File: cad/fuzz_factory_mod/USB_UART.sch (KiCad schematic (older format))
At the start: 14 parts, among them J301 USB_B_Micro, U301 USBLC6-2SC6, U302 FT230XS

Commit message: Continued schematic.
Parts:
- U301: footprint Package_TO_SOT_SMD:SOT-23-6 -> TO_SOT_Packages_SMD:SOT-23-6
- U302: footprint Package_SO:SSOP-16_3.9x4.9mm_P0.635mm -> Housings_SSOP:SSOP-16_3.9x4.9mm_Pitch0.635mm
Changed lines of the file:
@@
 $Descr A4 11693 8268
 encoding utf-8
-Sheet 3 22
+Sheet 3 26
 Title ""
 Date ""
@@
 F 0 "U302" H 5550 4150 50  0000 C CNN
 F 1 "FT230XS" H 6400 2950 50  0000 C CNN
-F 2 "Package_SO:SSOP-16_3.9x4.9mm_P0.635mm" H 6500 2900 50  0001 C CNN
+F 2 "Housings_SSOP:SSOP-16_3.9x4.9mm_Pitch0.635mm" H 6500 2900 50  0001 C CNN
 F 3 "http://www.ftdichip.com/Products/ICs/FT230X.html" H 6050 3550 50  0001 C CNN
 	1    6050 3550
@@
 F 0 "U301" V 2500 3750 50  0000 C CNN
 F 1 "USBLC6-2SC6" V 3200 3950 50  0000 C CNN
-F 2 "Package_TO_SOT_SMD:SOT-23-6" H 2100 3900 50  0001 C CNN
+F 2 "TO_SOT_Packages_SMD:SOT-23-6" H 2100 3900 50  0001 C CNN
 F 3 "http://www2.st.com/resource/en/datasheet/CD00050750.pdf" H 3050 3850 50  0001 C CNN
 	1    2850 3500

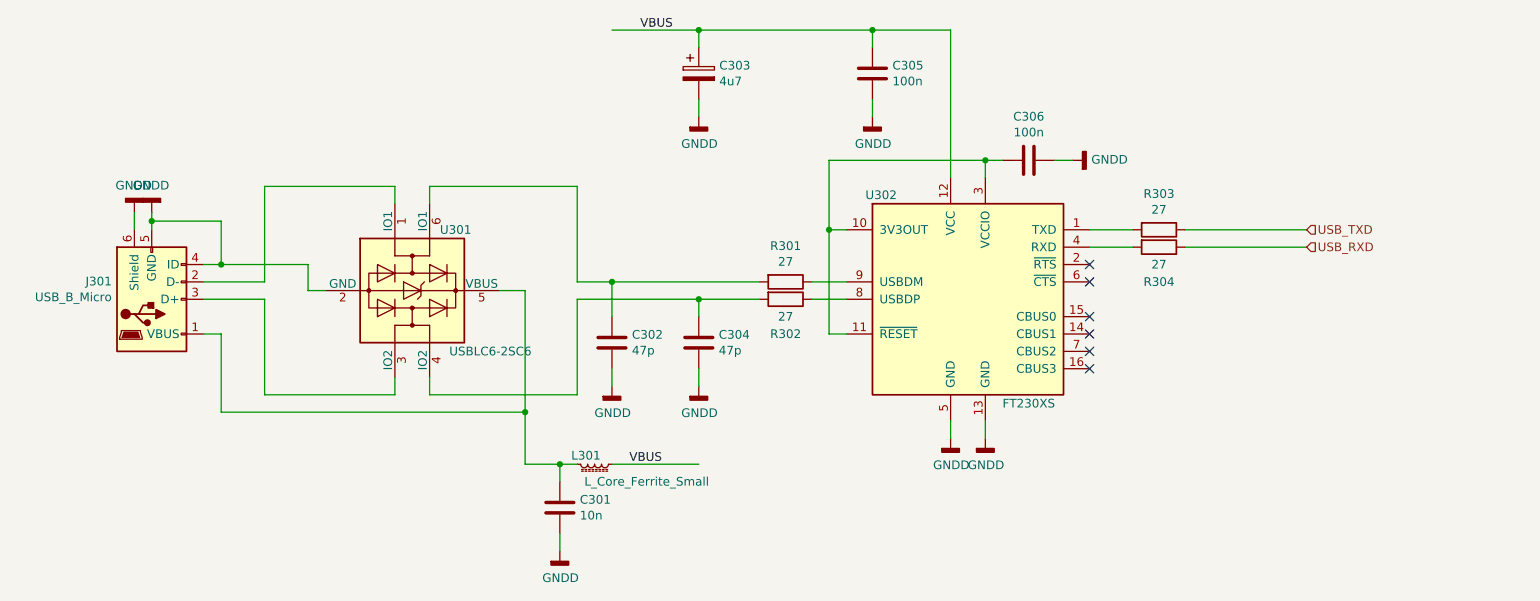
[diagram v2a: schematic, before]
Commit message: Changes architecture.
Corrections on schematic.
Continued Layout placement.
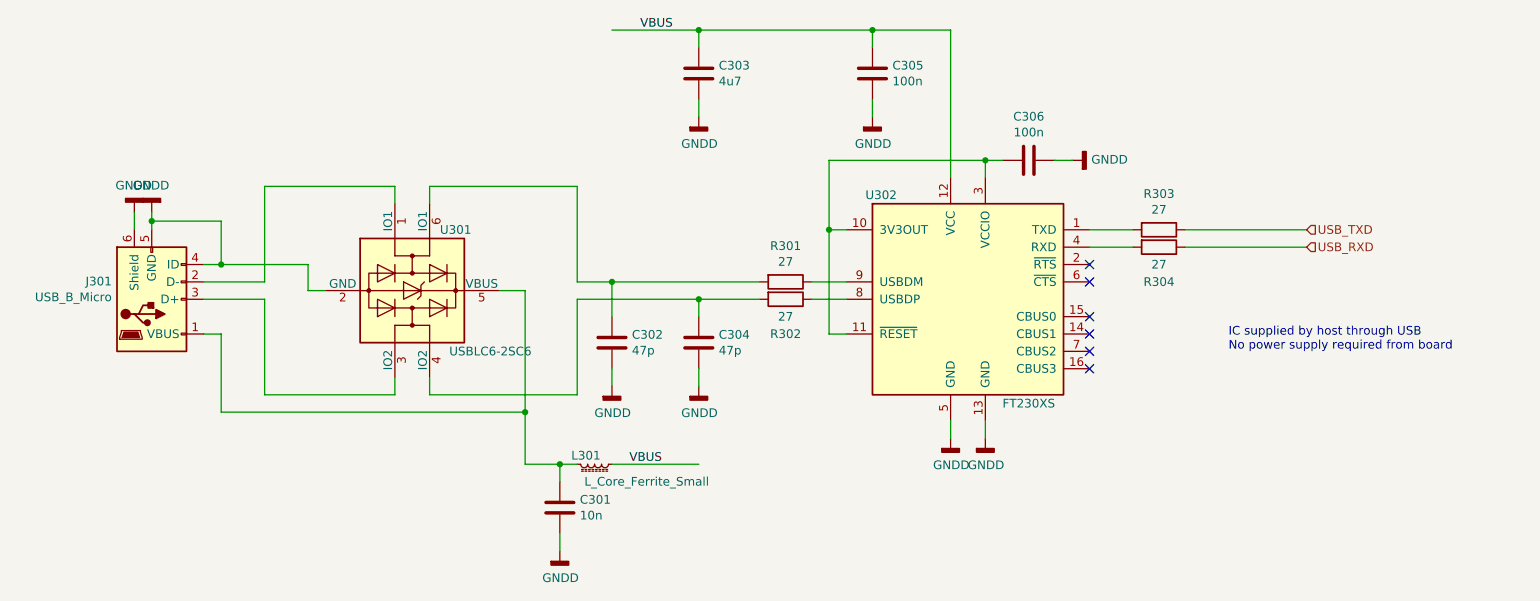
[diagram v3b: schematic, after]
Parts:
- removed C303: 4u7, Capacitors_SMD:CP_Elec_6.3x4.5, symbol Device:CP
- added C303: 4u7, Capacitors_SMD:C_1206, symbol Device:C
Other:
- note added: "IC supplied by host through USB\nNo power supply required from board"
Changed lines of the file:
@@
 $Descr A4 11693 8268
 encoding utf-8
-Sheet 3 30
+Sheet 3 22
 Title ""
 Date ""
@@
 F 3 "~" H 3700 4750 50  0001 C CNN
 	1    3700 4750
-	1    0    0    -1
-$EndComp
-$Comp
-L Device:CP C303
-U 1 1 5EB155B4
-P 4500 2250
-F 0 "C303" H 4618 2296 50  0000 L CNN
-F 1 "4u7" H 4618 2205 50  0000 L CNN
-F 2 "Capacitors_SMD:CP_Elec_6.3x4.5" H 4538 2100 50  0001 C CNN
-F 3 "~" H 4500 2250 50  0001 C CNN
-	1    4500 2250
 	1    0    0    -1
 $EndComp
@@
 Wire Wire Line
 	3800 3550 4500 3550
+Text Notes 7550 3850 0    50   ~ 0
+IC supplied by host through USB\nNo power supply required from board
+$Comp
+L Device:C C303
+U 1 1 5F265772
+P 4500 2250
+F 0 "C303" H 4615 2296 50  0000 L CNN
+F 1 "4u7" H 4615 2205 50  0000 L CNN
+F 2 "Capacitors_SMD:C_1206" H 4538 2100 50  0001 C CNN
+F 3 "~" H 4500 2250 50  0001 C CNN
+	1    4500 2250
+	1    0    0    -1
+$EndComp
 $EndSCHEMATC

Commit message: Continued layout.
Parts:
- U301: symbol Power_Protection:USBLC6-2SC6 -> fuzz_factory_mod-rescue:USBLC6-2SC6-Power_Protection
- U302: symbol Interface_USB:FT230XS -> fuzz_factory_mod-rescue:FT230XS-Interface_USB
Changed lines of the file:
@@
 EESchema Schematic File Version 4
-LIBS:fuzz_factory_mod-cache
 EELAYER 30 0
 EELAYER END
@@
 $EndDescr
 $Comp
-L Interface_USB:FT230XS U302
+L fuzz_factory_mod-rescue:FT230XS-Interface_USB U302
 U 1 1 5EB01C76
 P 6050 3550
+AR Path="/5EB01C76" Ref="U302"  Part="1"
+AR Path="/5DE4AD26/5EB00B3E/5EB01C76" Ref="U302"  Part="1"
 F 0 "U302" H 5550 4150 50  0000 C CNN
 F 1 "FT230XS" H 6400 2950 50  0000 C CNN
@@
 USB_TXD
 $Comp
-L Power_Protection:USBLC6-2SC6 U301
+L fuzz_factory_mod-rescue:USBLC6-2SC6-Power_Protection U301
 U 1 1 5EB33269
 P 2850 3500
